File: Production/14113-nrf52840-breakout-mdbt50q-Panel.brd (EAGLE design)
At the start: 180.3 x 106.7 mm, 1314 parts, among them J104 CORTEX_DEBUG_PTH, J116 CORTEX_DEBUG_PTH, J128 CORTEX_DEBUG_PTH, J140 CORTEX_DEBUG_PTH, J20 CORTEX_DEBUG_PTH, J32 CORTEX_DEBUG_PTH, J44 CORTEX_DEBUG_PTH, J56 CORTEX_DEBUG_PTH, J68 CORTEX_DEBUG_PTH, J8 CORTEX_DEBUG_PTH, J80 CORTEX_DEBUG_PTH, J92 CORTEX_DEBUG_PTH, U1 MDBT50Q, U10 MDBT50Q, U11 MCP73831, U12 3.3V, U13 MDBT50Q, U14 MCP73831, U15 3.3V, U16 MDBT50Q, U17 MCP73831, U18 3.3V, U19 MDBT50Q, U2 MCP73831, U20 MCP73831, U21 3.3V, U22 MDBT50Q, U23 MCP73831, U24 3.3V, U25 MDBT50Q, U26 MCP73831, U27 3.3V, U28 MDBT50Q, U29 MCP73831, U3 3.3V, U30 3.3V, U31 MDBT50Q, U32 MCP73831, U33 3.3V, U34 MDBT50Q, U35 MCP73831, U36 3.3V, U4 MDBT50Q, U5 MCP73831, U6 3.3V, U7 MDBT50Q, U8 MCP73831, U9 3.3V, Y1 32.768kHz, Y10 32.768kHz, Y11 32.768kHz, Y12 32.768kHz, Y2 32.768kHz, Y3 32.768kHz, Y4 32.768kHz, Y5 32.768kHz, Y6 32.768kHz, Y7 32.768kHz, Y8 32.768kHz, Y9 32.768kHz

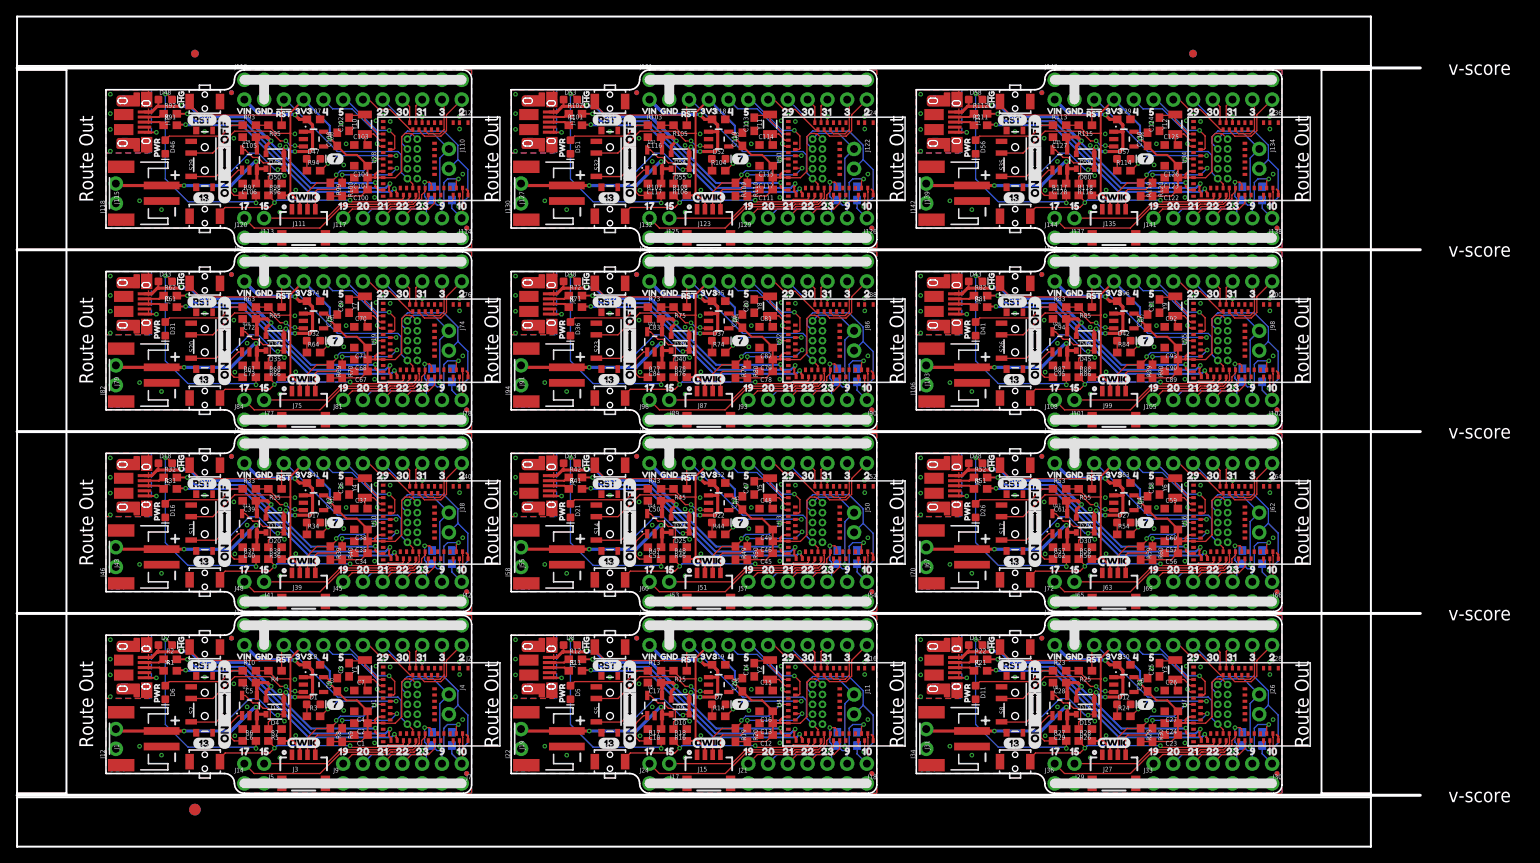
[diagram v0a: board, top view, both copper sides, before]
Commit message: Updated silk
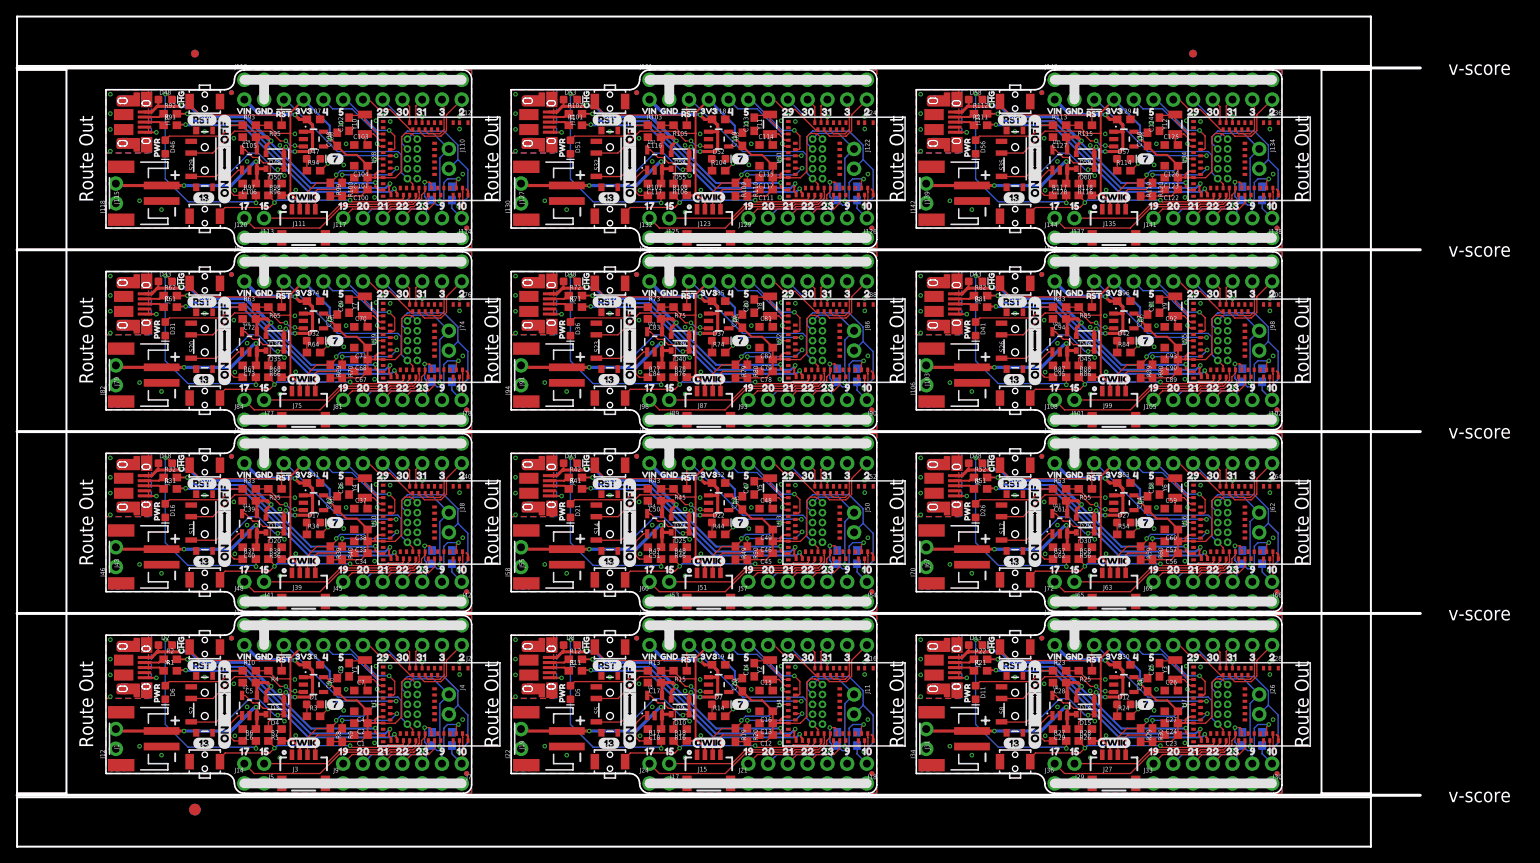
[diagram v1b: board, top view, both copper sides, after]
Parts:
- moved U$168 5.08 mm to (142.2, 15.0)
- moved U$342 5.08 mm to (142.2, 38.4)
- moved U$516 5.08 mm to (142.2, 61.7)
- moved U$690 5.08 mm to (142.2, 85.1)
- moved U$110 5.08 mm to (90.2, 15.0)
- moved U$226 5.08 mm to (38.1, 38.4)
- moved U$284 5.08 mm to (90.2, 38.4)
- moved U$35 5.08 mm to (38.1, 15.0)
- moved U$400 5.08 mm to (38.1, 61.7)
- moved U$458 5.08 mm to (90.2, 61.7)
- moved U$574 5.08 mm to (38.1, 85.1)
- moved U$632 5.08 mm to (90.2, 85.1)
- moved U$122 2.54 mm to (139.7, 15.0)
- moved U$296 2.54 mm to (139.7, 38.4)
- moved U$470 2.54 mm to (139.7, 61.7)
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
